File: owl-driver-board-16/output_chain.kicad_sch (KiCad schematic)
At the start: 20 parts, among them J4 1890963, Q2 AGM60P85AP, Q4 2N7002, U5 74LVC1G08

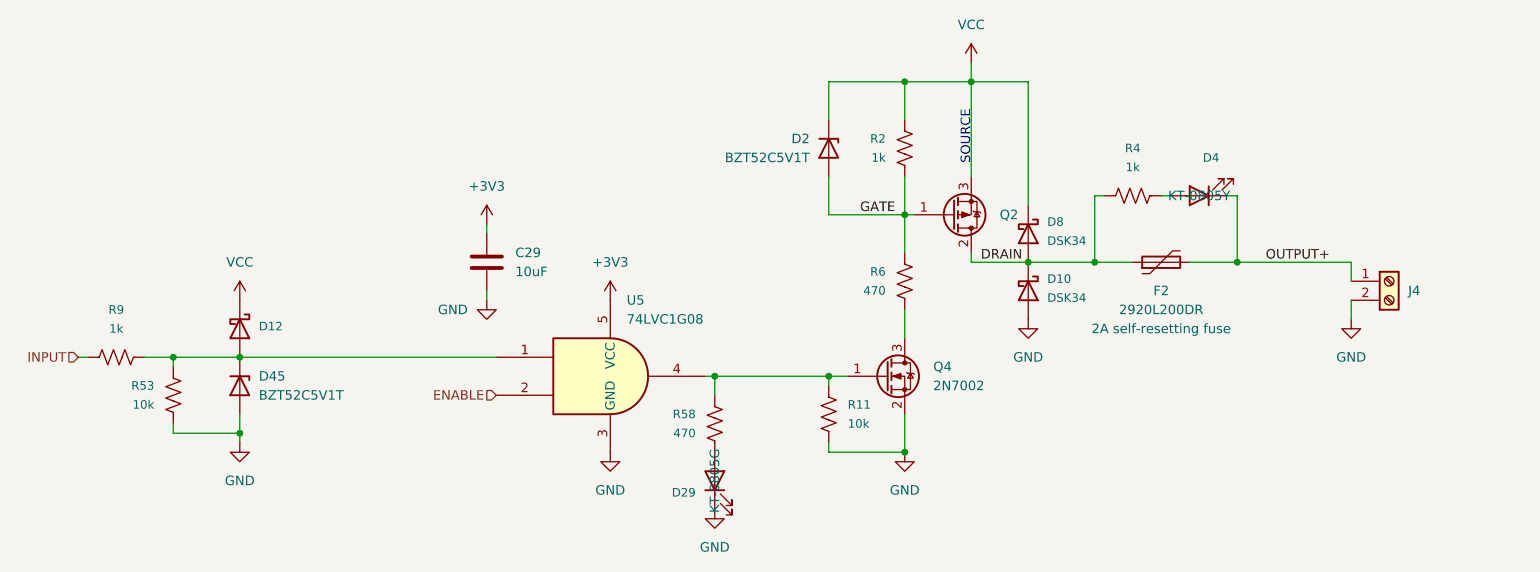
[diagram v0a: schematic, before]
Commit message: add 16-way board v1.1, with additional discharge resistor across outputs
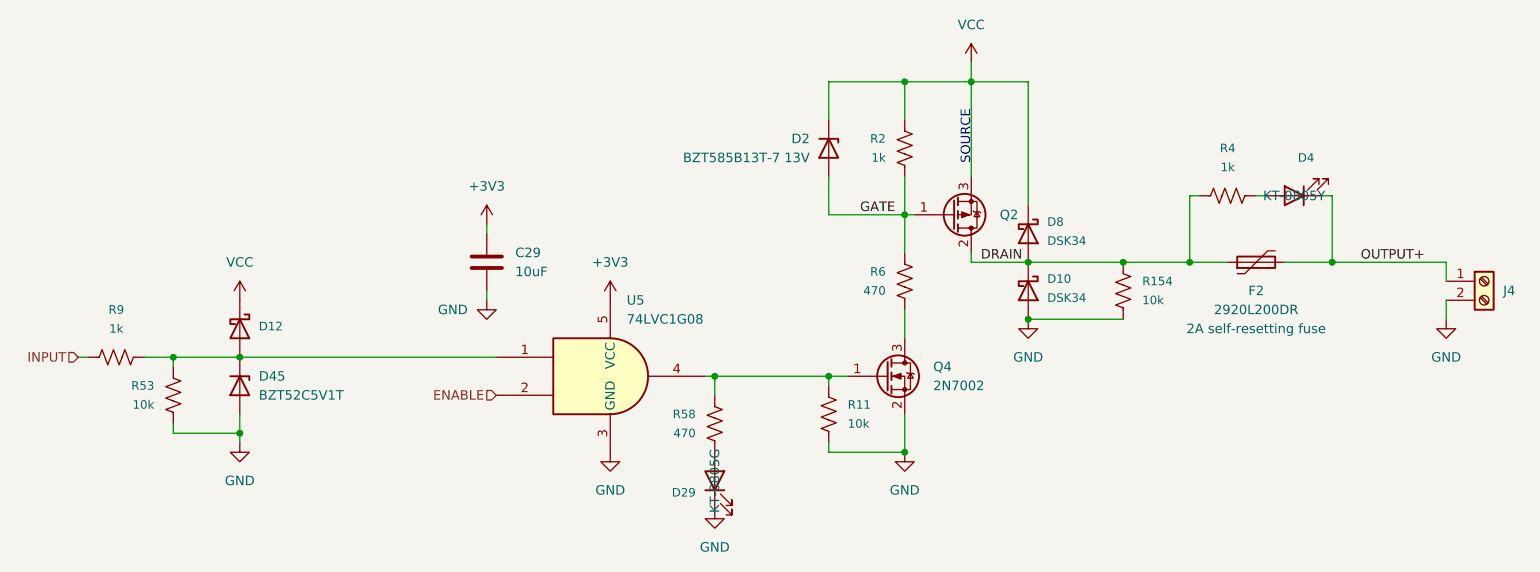
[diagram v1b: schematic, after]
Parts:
- added R154: 10k, Resistor_SMD:R_0603_1608Metric, symbol Device:R_US
- D2: value BZT52C5V1T -> BZT585B13T-7 13V; LCSC C2987034 -> C460799; Note 9V Zener -> (none); Part (none) -> BZT585B13T-7
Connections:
- net DRAIN: now also R154.2
- net GND: now also R154.1
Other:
- moved on the sheet: D4, F2, J4, R4
